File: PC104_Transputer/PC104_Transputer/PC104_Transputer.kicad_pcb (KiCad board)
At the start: 4 copper layers, 95.9 x 90.2 mm, 48 parts, among them J1 Conn_02x32_Odd_Even, J10 Conn_02x30_Row_Letter_First, J2 Conn_02x20_Odd_Even, J3 Conn_02x08_Odd_Even, J4 IRQDMA_JP, J5 Conn_02x05_Odd_Even, J9 Conn_02x30_Row_Letter_First, U1 ATF1502AS-xAx44, U11 IMSC011, U2 74LS244_Split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

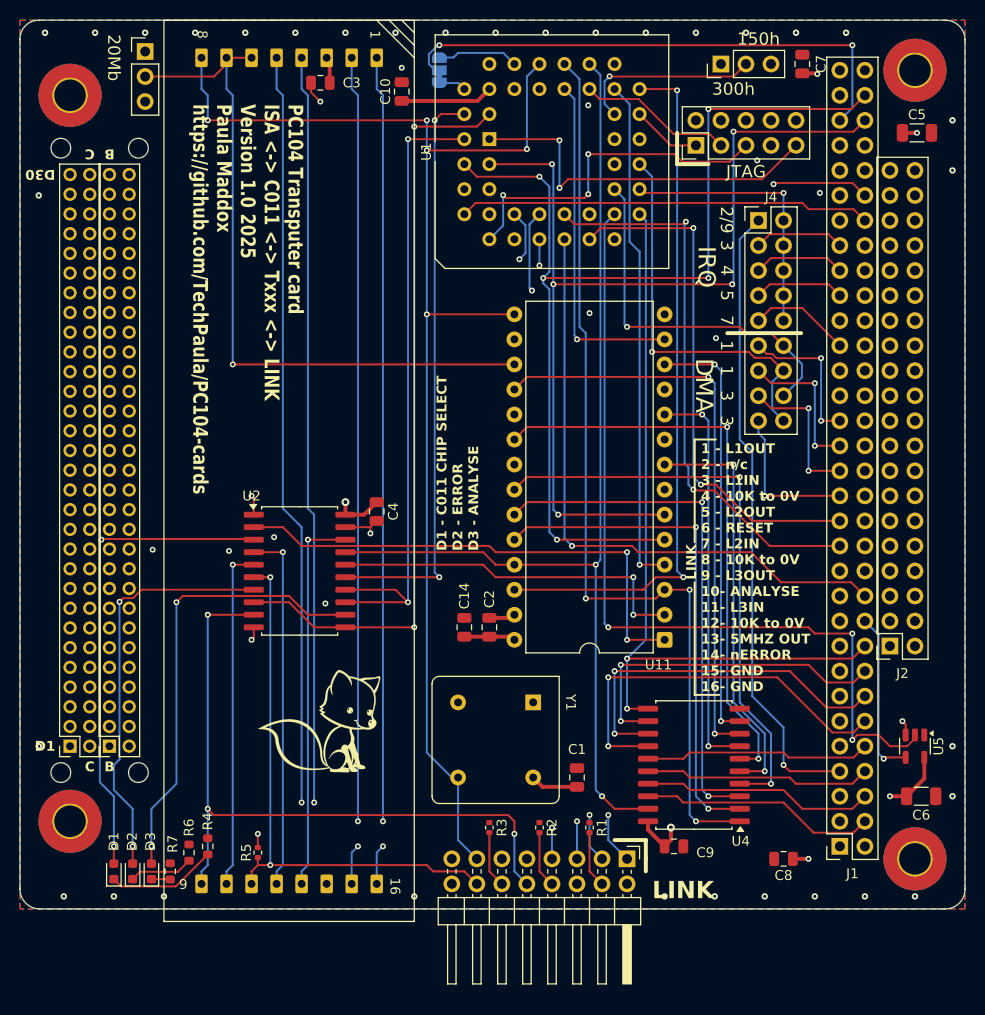
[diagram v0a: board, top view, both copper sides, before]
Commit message: Fixing a few things
Fixed a couple of minor things with the schematic and board for both cards
Also created Schematics
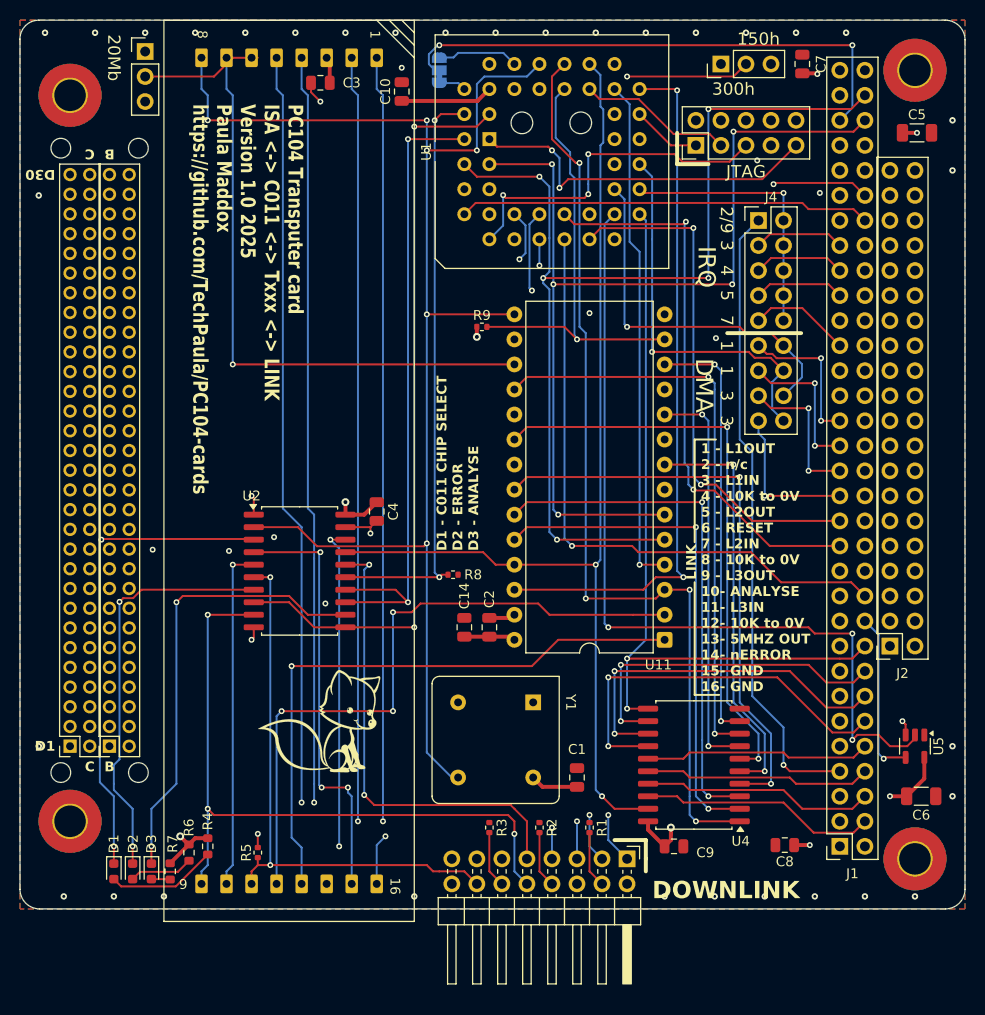
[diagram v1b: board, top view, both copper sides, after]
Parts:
- removed the FOX1 at (121.4, 118.2)
- added R8: 10K, Resistor_SMD:R_0402_1005Metric, F.Cu at (136.7, 103.3)
- added R9: 10K, Resistor_SMD:R_0402_1005Metric, F.Cu at (139.6, 78.1)
- added REF**: MountingHole_2.2mm_M2_DIN965, MountingHole:MountingHole_2.2mm_M2_DIN965, F.Cu at (149.6, 57.4)
- added REF**: MountingHole_2.2mm_M2_DIN965, MountingHole:MountingHole_2.2mm_M2_DIN965, F.Cu at (143.6, 57.4)
- moved C8 1.40 mm to (170.3, 130.7)
- turned D1 to -90 degrees
- turned D2 to -90 degrees
- turned D3 to -90 degrees
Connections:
- J3 pad 13: 5MHz -> Net-(J3-Pin_13)
- R4 pad 1: Net-(D1-K) -> Net-(D1-A)
- R4 pad 2: GND -> +5V
- R6 pad 1: Net-(D2-K) -> Net-(D2-A)
- R6 pad 2: GND -> +5V
- R7 pad 1: Net-(D3-K) -> Net-(D3-A)
- R7 pad 2: GND -> +5V
- U2 pad 12: Net-(D3-A) -> Net-(D3-K)
- U2 pad 16: Net-(U11-LinkIn) -> Net-(J3-Pin_9)
- U2 pad 18: Net-(U8-Link0in) -> Net-(J3-Pin_13)
- U2 pad 2: Net-(U11-LinkOut) -> 5MHz
- U2 pad 3: Net-(D1-A) -> Net-(D1-K)
- U2 pad 4: Net-(U8-Link0out) -> Net-(U8-Link3out)
- U2 pad 7: Net-(D2-A) -> Net-(D2-K)
- U8 pad 12: Net-(U8-Link0out) -> Net-(U11-LinkIn)
- U8 pad 13: Net-(U8-Link0in) -> Net-(U11-LinkOut)
- U8 pad 15: Net-(J3-Pin_9) -> Net-(U8-Link3out)
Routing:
- net Net-(J3-Pin_13): track 0.00 -> 47.7 mm, vias 0 -> 2
- net Net-(D3-K): track 1.92 -> 45.8 mm, vias 0 -> 2
- net Net-(D3-A): track 45.8 -> 1.92 mm, vias 2 -> 0
- net Net-(U8-Link3out): track 0.00 -> 43.4 mm, vias 0 -> 3
- net Net-(U8-Link0in): track 39.0 -> 0.00 mm, vias 1 -> 0
- net Net-(D1-K): track 11.2 -> 49.0 mm, vias 0 -> 2
- net Net-(D1-A): track 49.0 -> 11.2 mm, vias 2 -> 0
- net Net-(U8-Link0out): track 36.9 -> 0.00 mm, vias 1 -> 0
- net Net-(D2-K): track 6.49 -> 41.7 mm, vias 0 -> 2
- net Net-(D2-A): track 41.7 -> 6.49 mm, vias 2 -> 0
- net Net-(U11-LinkIn): track 36.7 -> 67.5 mm, vias 2 -> 3
- net Net-(J3-Pin_9): track 22.8 -> 47.4 mm, vias 1 -> 2
- net C011_RESET: track 34.8 -> 45.3 mm
- net Net-(U11-LinkOut): track 51.6 -> 61.5 mm, vias 2 -> 1
- net 5MHz: track 134.5 -> 143.6 mm, vias 5 -> 6
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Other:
- board text added: "DOWNLINK"

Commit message: Fixed CPLD pinout
Fixed the CPLD pin out which would never have worked with the previous version due to the PLCC and TQFP pinouts being different
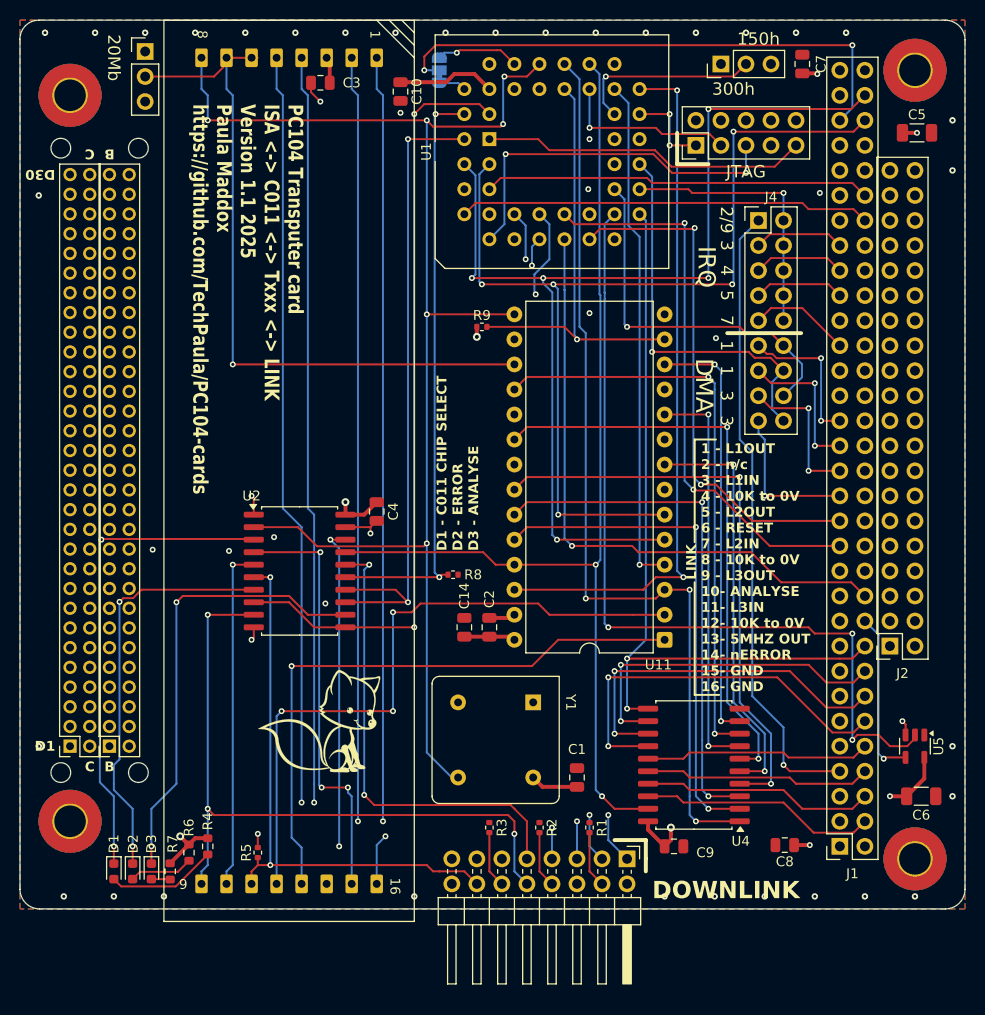
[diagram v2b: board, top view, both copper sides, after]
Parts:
- removed REF** (x2): MountingHole_2.2mm_M2_DIN965, MountingHole:MountingHole_2.2mm_M2_DIN965
- added FOX1: SYM_Flash_Large, PaulasKiCADFootPrint:Fox_avatar_18mm, B.Cu at (121.6, 118.3)
- moved C10 0.13 mm to (131.3, 54.2), turned to -90 degrees
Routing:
- net TDI: track 36.7 -> 33.2 mm, vias 2 -> 0
- net TDO: track 15.7 -> 18.0 mm, vias 0 -> 1
- net +5V: track 54.9 -> 52.6 mm
- net TMS: track 35.1 -> 37.3 mm, vias 3 -> 2
- net ADDR_SEL: track 16.9 -> 19.0 mm
- net 5MHz: track 143.6 -> 141.6 mm
- net TCK: track 7.03 -> 8.89 mm, vias 0 -> 2
- net nPC_ANALYSE: track 76.3 -> 77.9 mm
- net RS1: track 100.5 -> 102.0 mm
- net R/nW: track 95.5 -> 94.2 mm, vias 4 -> 3
- net ISA_CLK: track 53.8 -> 55.0 mm
- net /AD8: track 37.1 -> 38.1 mm
- net /AD7: track 40.8 -> 40.0 mm
- net C011_RESET: track 45.3 -> 44.5 mm
- net Net-(JP3-B): track 8.28 -> 8.50 mm, vias 0 -> 1
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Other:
- board text added: "PC104 Transputer card ISA <-> C011 <-> Txxx <-> LINK Version 1.1 2025 Paula Maddox https://github.com/TechPaula/PC104-cards"
- board text removed: "PC104 Transputer card ISA <-> C011 <-> Txxx <-> LINK Version 1.0 2025 Paula Maddox https://github.com/TechPaula/PC104-cards"

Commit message: Fixed error with PCB, added CPLD files
CPLD files tested on breadboard with a bunch of wires. PCB mistake fixed.
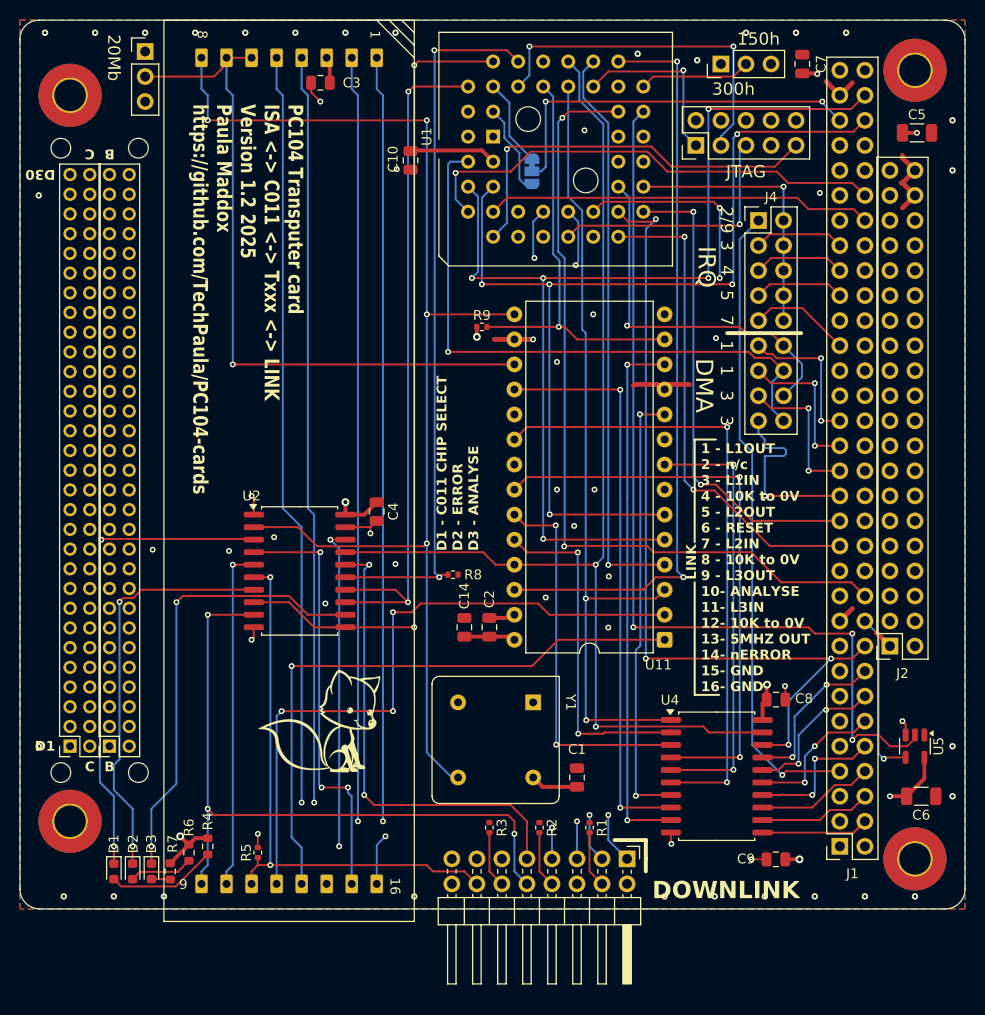
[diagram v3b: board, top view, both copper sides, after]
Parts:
- added H1: MountingHole, MountingHole:MountingHole_2.5mm, F.Cu at (144.3, 57.0)
- added H2: MountingHole, MountingHole:MountingHole_2.5mm, F.Cu at (150.1, 63.2)
- U1: value ATF1502AS-xAx44 -> ~
- moved C8 14.8 mm to (169.4, 115.9), turned to 0 degrees
- moved JP3 13.9 mm to (144.7, 62.3), turned to -90 degrees
- moved C9 10.4 mm to (169.4, 132.1), turned to 180 degrees
- moved C10 7.06 mm to (132.3, 61.2)
- moved U4 2.58 mm to (163.4, 123.7), turned to 0 degrees
- moved FOX1 1.49 mm to (123.1, 118.1)
- moved U1 0.46 mm to (140.7, 58.8)
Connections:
- U1 pad 1: TDI -> unconnected-(U1-I/GCLR-Pad1)
- U1 pad 10: /AD7 -> GND
- U1 pad 11: /AD8 -> unconnected-(U1-I/O/PD1-Pad11)
- U1 pad 12: /AD9 -> /AD7
- U1 pad 13: AEN -> TMS
- U1 pad 14: nIOW -> /AD8
- U1 pad 15: nIOR -> +5V
- U1 pad 16: GND -> /AD9
- U1 pad 17: +5V -> nIOW
- U1 pad 18: DB0 -> nIOR
- U1 pad 19: nRI/OCHRDY -> DB0
- U1 pad 2: RS0 -> DACK
- U1 pad 22: DACK -> GND
- U1 pad 23: unconnected-(U1-I/O-Pad23) -> +5V
- U1 pad 24: GND -> unconnected-(U1-I/O-Pad24)
- U1 pad 26: TCK -> nRI/OCHRDY
- U1 pad 27: ADDR_SEL -> AEN
- U1 pad 28: INPUT_INT -> ADDR_SEL
- U1 pad 29: +5V -> INPUT_INT
- U1 pad 3: RS1 -> +5V
- U1 pad 30: OUTPUT_INT -> GND
- U1 pad 31: nCS -> OUTPUT_INT
- U1 pad 32: TDO -> TCK
- U1 pad 33: R/nW -> nCS
- U1 pad 34: C011_RESET -> R/nW
- U1 pad 35: 5MHz -> +5V
- U1 pad 36: GND -> C011_RESET
- U1 pad 37: Net-(JP3-B) -> nPC_RESET
- U1 pad 38: unconnected-(U1-I/OE1/Vpp-Pad38) -> TDO
- U1 pad 39: unconnected-(U1-I/GCLR-Pad39) -> nPC_ANALYSE
- U1 pad 4: GND -> RS0
- U1 pad 40: Net-(JP3-A) -> nPC_ERROR
- U1 pad 41: +5V -> Net-(JP3-A)
- U1 pad 42: nPC_RESET -> GND
- U1 pad 43: nPC_ANALYSE -> Net-(JP3-B)
- U1 pad 44: nPC_ERROR -> unconnected-(U1-I/OE1-Pad44)
- U1 pad 5: /AD4 -> RS1
- U1 pad 6: /AD5 -> /AD4
- U1 pad 7: TMS -> TDI
- U1 pad 8: /AD6 -> /AD5
- U1 pad 9: +5V -> /AD6
- U4 pad 11: DB0 -> /PC104Connectors/DB7
- U4 pad 12: /PC104Connectors/DB1 -> /PC104Connectors/DB6
- U4 pad 13: /PC104Connectors/DB2 -> /PC104Connectors/DB5
- U4 pad 14: /PC104Connectors/DB3 -> /PC104Connectors/DB4
- U4 pad 15: /PC104Connectors/DB4 -> /PC104Connectors/DB3
- U4 pad 16: /PC104Connectors/DB5 -> /PC104Connectors/DB2
- U4 pad 17: /PC104Connectors/DB6 -> /PC104Connectors/DB1
- U4 pad 18: /PC104Connectors/DB7 -> DB0
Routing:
- net GND: track 11.3 -> 65.2 mm, vias 48 -> 55
- net /PC104Connectors/DB3: track 39.8 -> 14.5 mm
- net DACK: track 39.7 -> 62.0 mm
- net /PC104Connectors/DB2: track 37.2 -> 15.2 mm
- net AEN: track 63.3 -> 82.5 mm, vias 1 -> 2
- net /PC104Connectors/DB1: track 34.5 -> 16.3 mm
- net TDO: track 18.0 -> 35.8 mm, vias 1 -> 2
- net 5MHz: track 141.6 -> 124.6 mm, vias 6 -> 4
- net Net-(U11-D0): track 51.2 -> 34.8 mm
- net ISA_CLK: track 55.0 -> 38.9 mm
- net Net-(U11-D1): track 52.9 -> 38.6 mm
- net +5V: track 52.6 -> 66.8 mm
- net /PC104Connectors/DB7: track 24.0 -> 10.9 mm
- net nPC_RESET: track 60.7 -> 73.2 mm
- net R/nW: track 94.2 -> 82.0 mm, vias 3 -> 2
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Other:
- board text added: "GCLK3"
- board text added: "PC104 Transputer card ISA <-> C011 <-> Txxx <-> LINK Version 1.2 2025 Paula Maddox https://github.com/TechPaula/PC104-cards"
- board text removed: "GCLK2"
- board text removed: "PC104 Transputer card ISA <-> C011 <-> Txxx <-> LINK Version 1.1 2025 Paula Maddox https://github.com/TechPaula/PC104-cards"

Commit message: Added extra jumpers to transputer board
I also moved the downstream link to the same place as the upstream on the dual TRAM card.
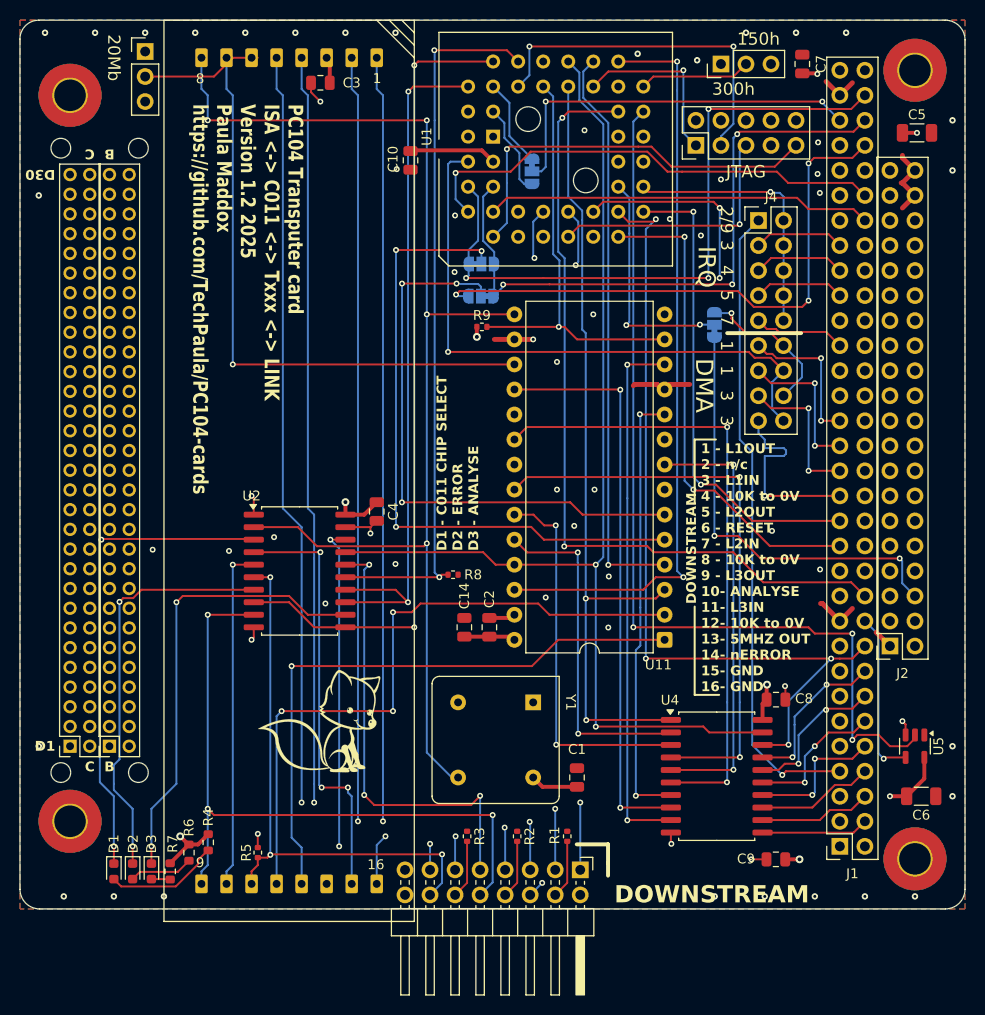
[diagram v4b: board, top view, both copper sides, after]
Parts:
- added JP4: Jumper_3_Bridged12, Jumper:SolderJumper-3_P1.3mm_Bridged12_RoundedPad1.0x1.5mm_NumberLabels, B.Cu at (163.2, 77.9)
- added JP5: Jumper_3_Bridged12, Jumper:SolderJumper-3_P1.3mm_Bridged12_RoundedPad1.0x1.5mm_NumberLabels, B.Cu at (139.5, 71.7)
- added JP6: Jumper_3_Bridged12, Jumper:SolderJumper-3_P1.3mm_Bridged12_RoundedPad1.0x1.5mm_NumberLabels, B.Cu at (139.5, 75.0)
- moved J3 4.88 mm to (149.6, 133.2)
- moved R1 2.43 mm to (148.2, 129.8)
- moved R3 2.43 mm to (138.1, 129.8)
- moved R2 2.43 mm to (143.2, 129.8)
- moved R4 0.41 mm to (111.8, 130.4)
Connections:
- J1 pad 60: RS1 -> /AD1
- J1 pad 62: RS0 -> /AD0
- J2 pad 6: unconnected-(J2-Pin_6-Pad6) -> nIOCS16
- U1 pad 21: DRQ -> Net-(JP4-C)
- U1 pad 4: RS0 -> /AD0
- U1 pad 5: RS1 -> /AD1
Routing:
- net /AD0: track 0.00 -> 68.4 mm, vias 0 -> 3
- net /AD1: track 0.00 -> 65.8 mm, vias 0 -> 3
- net /AD2: track 0.00 -> 58.5 mm, vias 0 -> 3
- net nIOCS16: track 0.00 -> 44.3 mm, vias 0 -> 2
- net RS1: track 99.8 -> 58.5 mm, vias 5 -> 3
- net RS0: track 106.4 -> 65.9 mm, vias 5 -> 3
- net Net-(JP4-C): track 0.00 -> 23.6 mm, vias 0 -> 2
- net DRQ: track 38.1 -> 15.4 mm
- net Net-(J3-Pin_5): track 101.2 -> 97.4 mm
- net Net-(J3-Pin_7): track 100.9 -> 97.2 mm
- net Net-(J3-Pin_13): track 47.7 -> 45.0 mm, vias 2 -> 3
- net GND: track 65.2 -> 67.9 mm, vias 55 -> 61
- net Net-(J3-Pin_3): track 111.3 -> 108.8 mm
- net Net-(J3-Pin_11): track 18.0 -> 15.7 mm, vias 1 -> 2
- net Net-(J3-Pin_1): track 111.7 -> 109.9 mm
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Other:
- board text added: "DOWNSTREAM"
- board text added: "for 16 bit transfer JP4, JP5 and JP6 pins 1&2 should be cut, and pins 2&3 should be shorted"
- board text removed: "DOWNLINK"
- board text removed: "LINK"
